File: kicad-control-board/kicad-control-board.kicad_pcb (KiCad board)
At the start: 2 copper layers, 100 x 110 mm, 97 parts, among them J1 Conn_01x10_Female, J2 Conn_01x16_Male, J3 BA56_3DIG_7SEG, J4 Gate Out, J5 Clock Out, J6 Clock In, J7 Pitch Out, J8 CV Out, J9 Reset In, Q1 2N3906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

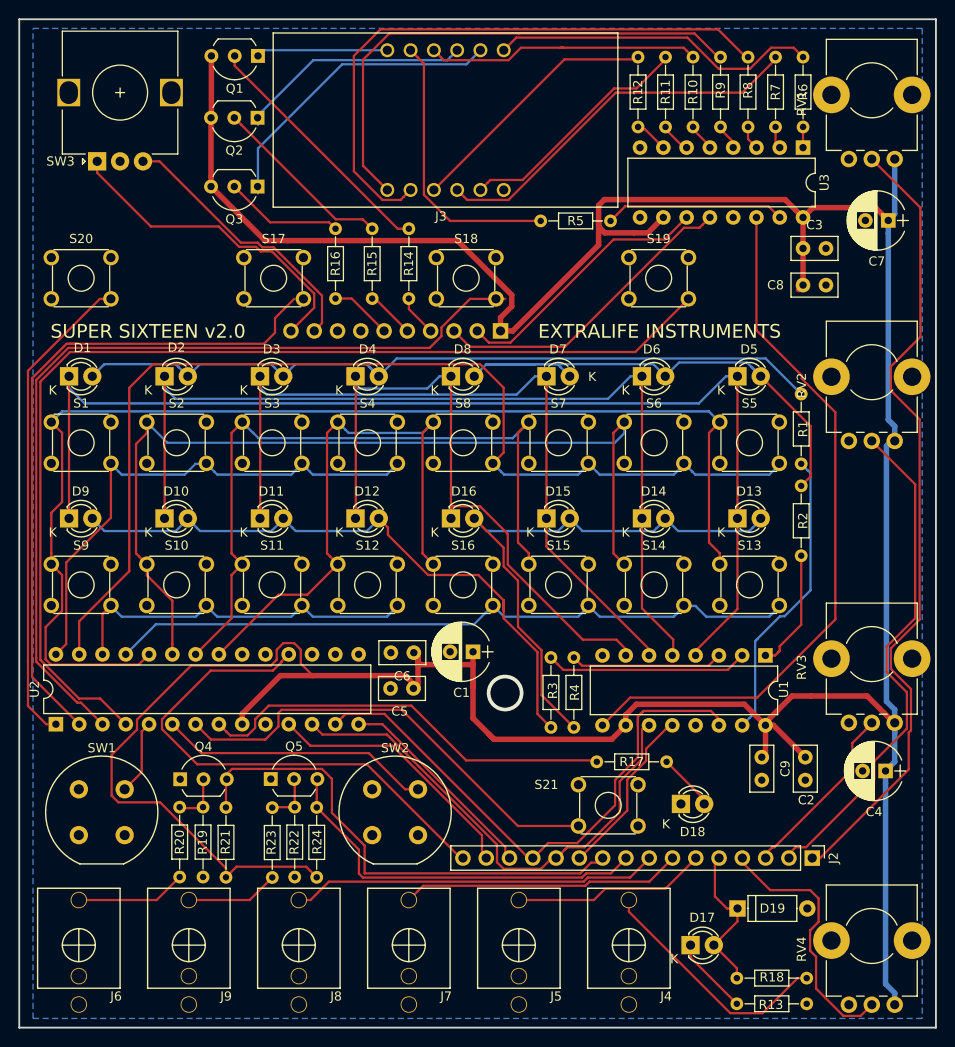
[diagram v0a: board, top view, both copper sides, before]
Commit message: Updating control positions, adding standoff on control PCB
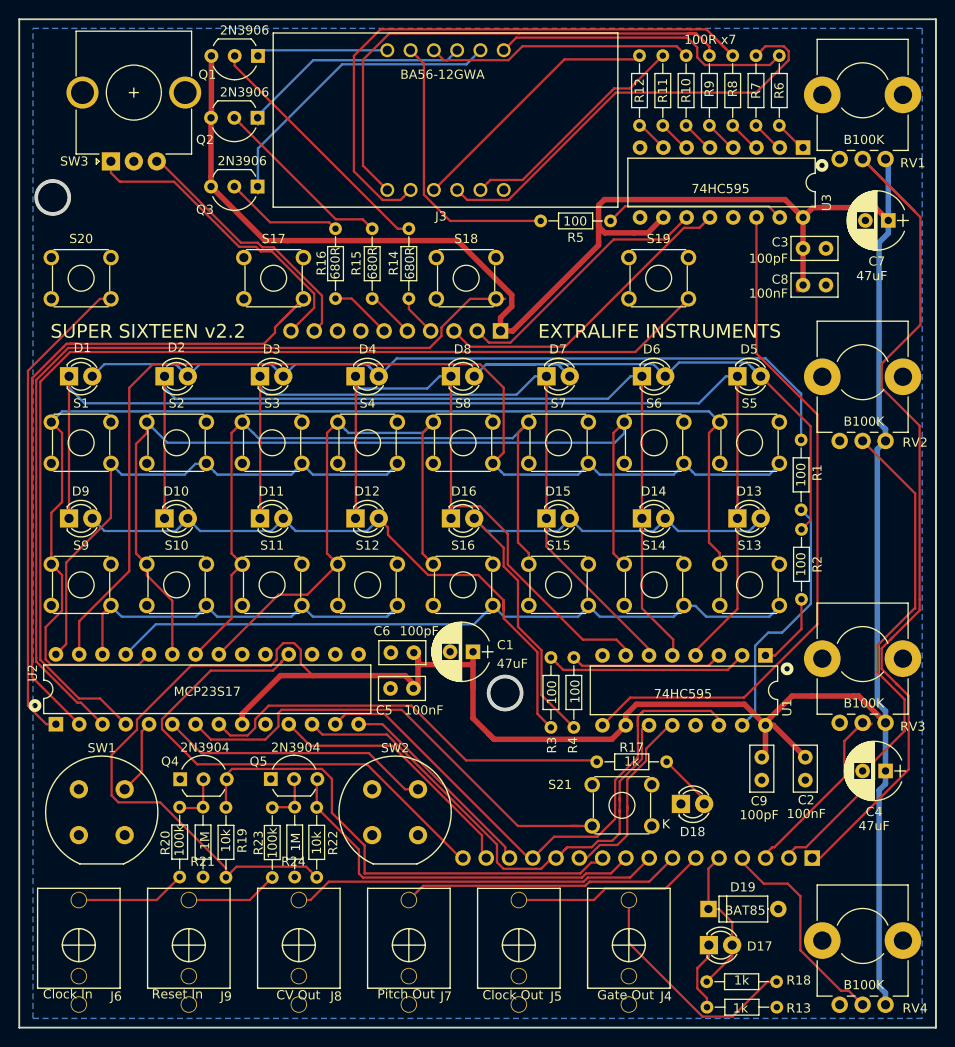
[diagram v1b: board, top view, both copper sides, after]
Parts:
- added REF***: WEEE-Logo_5.6x8mm_SilkScreen, Symbols:WEEE-Logo_5.6x8mm_SilkScreen, B.Cu at (51.8, 23.1)
- added REF***: OSHW-Logo2_7.3x6mm_SilkScreen, Symbols:OSHW-Logo2_7.3x6mm_SilkScreen, B.Cu at (64.0, 22.9)
- J2: moved to B.Cu
- J3: value BA56_3DIG_7SEG -> BA56-12GWA
- R14, R15, R16: value 660 -> 680R
- R6: value 100 -> 100R x7
- moved R1 5.01 mm to (97.3, 65.5)
- moved R2 4.75 mm to (97.3, 67.7)
- moved R18 3.31 mm to (94.6, 117.0)
- moved R13 3.28 mm to (94.6, 119.8)
- moved D19 3.17 mm to (87.2, 109.1)
- moved R6 2.59 mm to (94.9, 23.6)
- moved R7 2.14 mm to (92.4, 23.6)
- moved D17 2.00 mm to (88.5, 113.0)
- moved R8 1.68 mm to (89.8, 23.6)
- moved S21 1.50 mm to (81.0, 100.0)
- moved SW3 1.50 mm to (22.0, 27.5)
- moved R9 1.23 mm to (87.3, 23.6)
- moved RV1 1.00 mm to (106.5, 27.2)
- moved RV2 1.00 mm to (106.5, 58.0)
- moved RV3 1.00 mm to (106.5, 88.8)
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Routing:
- net AD1: track 88.7 -> 99.3 mm
- net Net-(J3-Pad4): track 41.5 -> 48.1 mm
- net Net-(D1-Pad2): track 84.5 -> 89.8 mm
- net AD4: track 28.9 -> 23.7 mm
- net Net-(D5-Pad2): track 59.3 -> 64.1 mm
- net Net-(R2-Pad2): track 13.1 -> 8.37 mm
- net Net-(R1-Pad1): track 32.5 -> 27.9 mm
- net /A1: track 73.8 -> 77.8 mm
- net Net-(J3-Pad7): track 36.0 -> 32.9 mm
- net Net-(U1-Pad9): track 77.6 -> 75.1 mm
- net /A6: track 49.9 -> 52.2 mm
- net Net-(R7-Pad1): track 2.19 -> 4.24 mm
- net ENC2: track 29.8 -> 28.0 mm
- net Net-(R9-Pad1): track 2.57 -> 4.21 mm
- net Net-(R6-Pad1): track 2.00 -> 3.59 mm
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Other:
- board text added: "SUPER SIXTEEN v2.2"
- board text removed: "SUPER SIXTEEN v2.0"
